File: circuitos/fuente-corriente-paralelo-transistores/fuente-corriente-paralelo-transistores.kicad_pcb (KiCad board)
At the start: 2 copper layers, 20 parts, among them J2 Conn_01x04_Pin, J3 Conn_01x04_Pin, U1 LM324, U2 Pico, U3 LM324

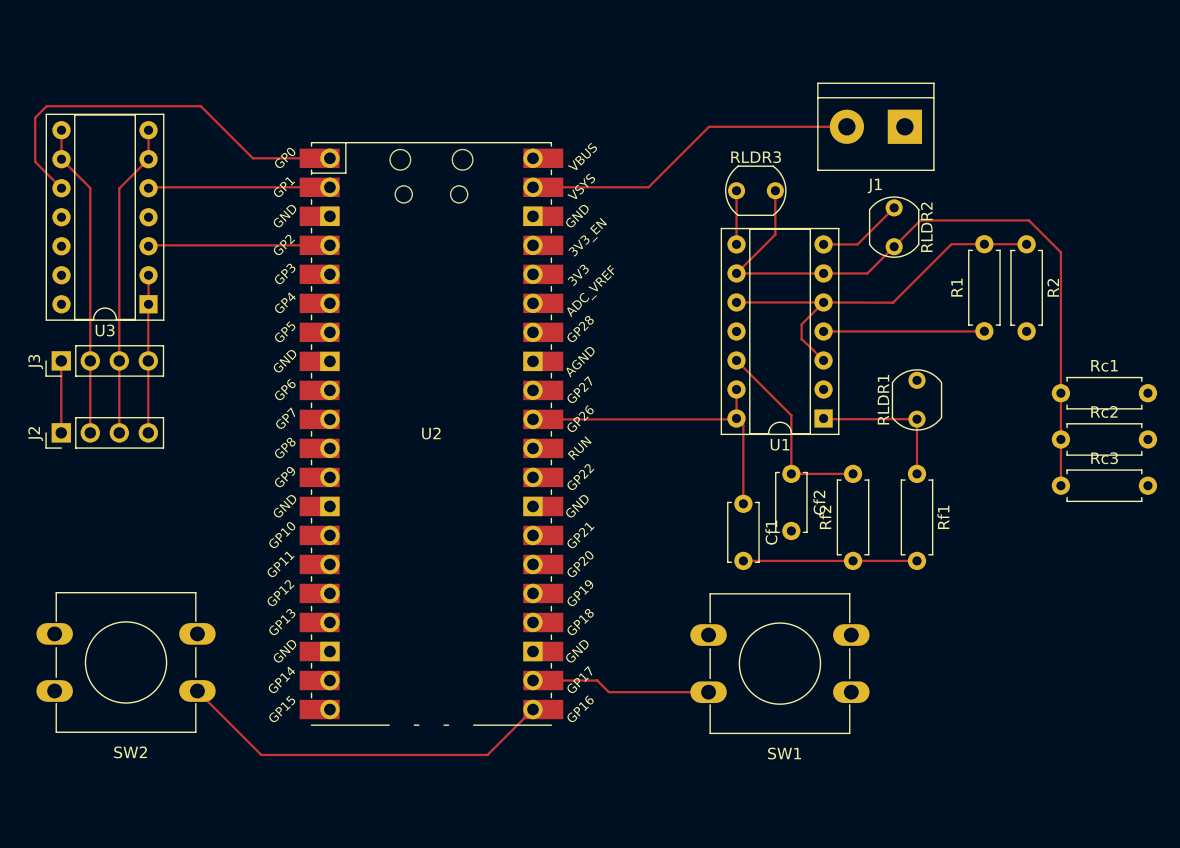
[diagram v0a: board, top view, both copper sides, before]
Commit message: pcb con LDRs y led ws2812b-mini
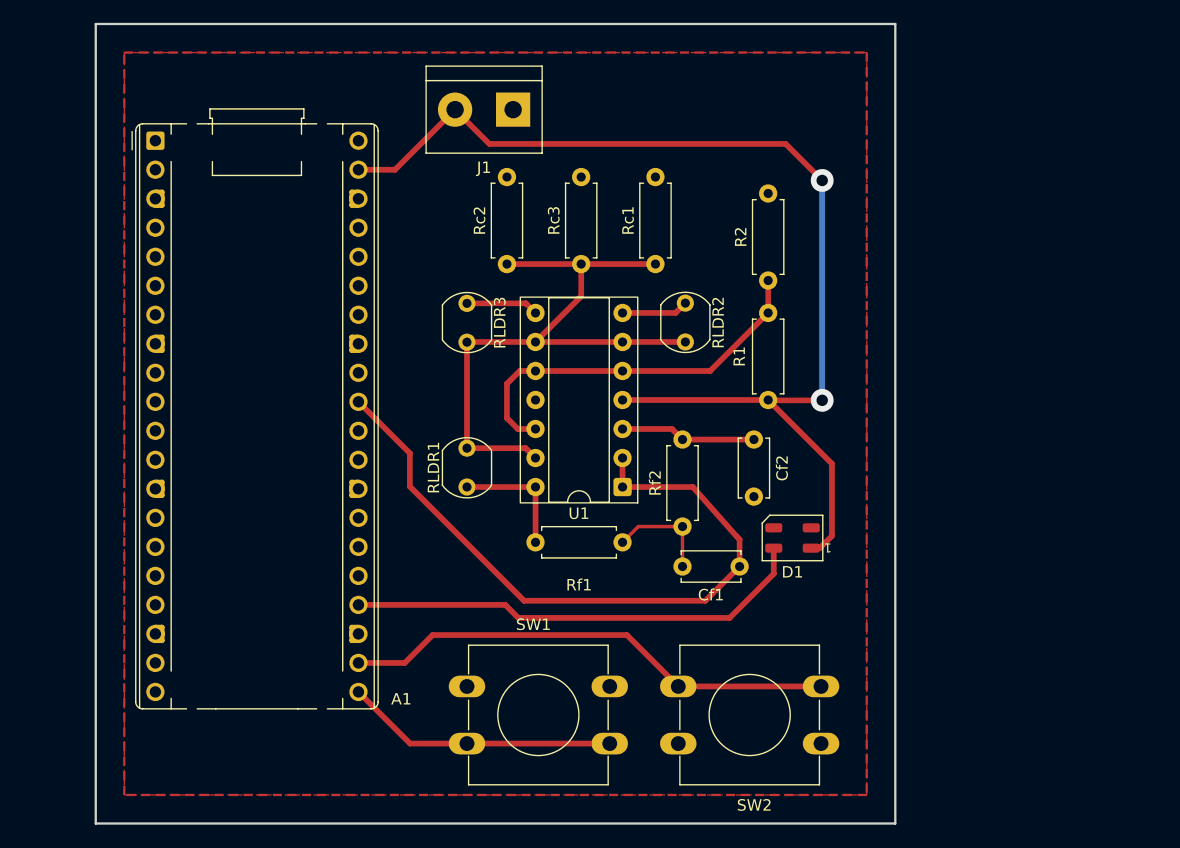
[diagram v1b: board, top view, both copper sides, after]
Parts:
- removed J2, J3: Conn_01x04_Pin, Connector_PinHeader_2.54mm:PinHeader_1x04_P2.54mm_Vertical
- removed U2: Pico, MCU_RaspberryPi_and_Boards:RPi_Pico_SMD_TH
- removed U3: LM324, Package_DIP:DIP-14_W7.62mm_Socket
- added A1: RaspberryPi_Pico_W, Module:RaspberryPi_Pico_Common_THT, F.Cu at (85.7, 57.2)
- added D1: WS2812B, LED_SMD:LED_WS2812B-Mini_PLCC4_3.5x3.5mm, F.Cu at (141.5, 92.0)
- SW1, SW2: value ~ -> SW_Push
- moved SW2 54.8 mm to (144.0, 110.0)
- moved Rc2 50.9 mm to (116.5, 68.0), turned to 90 degrees
- moved Rc3 46.3 mm to (123.0, 68.0), turned to 90 degrees
- moved RLDR1 39.8 mm to (113.0, 87.5)
- moved Rc1 37.3 mm to (129.5, 68.0), turned to 90 degrees
- moved J1 34.3 mm to (117.0, 54.5)
- moved Rf1 33.9 mm to (119.0, 92.4), turned to 0 degrees
- moved SW1 33.7 mm to (113.0, 105.0), turned to 0 degrees
- moved RLDR3 25.6 mm to (113.0, 71.5), turned to -90 degrees
- moved R2 22.9 mm to (139.4, 69.5), turned to 90 degrees
- moved RLDR2 20.1 mm to (132.1, 71.4)
- moved R1 19.9 mm to (139.4, 79.9)
- moved U1 18.6 mm to (126.6, 87.5)
- moved Rf2 15.2 mm to (131.9, 91.0)
- moved Cf1 5.50 mm to (136.9, 94.5), turned to 180 degrees
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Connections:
- Cf2 pad 1: Net-(U1D-+) -> Net-(U1A-+)
- RLDR1 pad 2: Net-(U1A--) -> Net-(U1B--)
- RLDR2 pad 2: Net-(U1A--) -> Net-(U1B--)
- RLDR3 pad 2: Net-(U1A--) -> Net-(U1B--)
- Rc1 pad 1: Net-(U1A--) -> Net-(U1B--)
- Rc2 pad 1: Net-(U1A--) -> Net-(U1B--)
- Rc3 pad 1: Net-(U1A--) -> Net-(U1B--)
- Rf2 pad 2: Net-(U1D-+) -> Net-(U1A-+)
- SW1 pad 1: /Btn1 -> GND
- SW2 pad 1: /Btn2 -> GND
- U1 pad 1: /Vldr -> /Vfiltrado
- U1 pad 12: Net-(U1D-+) -> /sensores/Vref
- U1 pad 13: /Vfiltrado -> Net-(U1B--)
- U1 pad 14: /Vfiltrado -> /Vldr
- U1 pad 2: Net-(U1A--) -> /Vfiltrado
- U1 pad 3: /sensores/Vref -> Net-(U1A-+)
- U1 pad 6: Net-(U1A--) -> Net-(U1B--)
- U1 pad 9: Net-(U1A--) -> Net-(U1B--)
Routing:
- net Net-(U1A--): track 60.6 -> 0.00 mm
- net Net-(U1B--): track 0.00 -> 56.2 mm
- net VCC: track 43.8 -> 98.6 mm, vias 0 -> 2
- net /Vled: track 0.00 -> 40.7 mm
- net /VledR: track 35.2 -> 0.00 mm
- net /Vfiltrado: track 28.1 -> 60.8 mm
- net Net-(J2-Pin_2): track 27.6 -> 0.00 mm
- net Net-(J2-Pin_3): track 27.6 -> 0.00 mm
- net Net-(U1D-+): track 17.3 -> 0.00 mm
- net /VledG: track 15.9 -> 0.00 mm
- net /VledB: track 15.9 -> 0.00 mm
- net Net-(J2-Pin_4): track 13.8 -> 0.00 mm
- net Net-(U1A-+): track 0.00 -> 11.9 mm
- net /Btn2: track 33.3 -> 43.4 mm
- net /Btn1: track 15.8 -> 23.9 mm
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- added copper zone on F.Cu, net GND
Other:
- board outline added: 70 x 70 mm
